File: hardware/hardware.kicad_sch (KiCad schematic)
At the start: 34 parts, among them J1 Conn_01x02, Q1 AON6500, Q2 AON6500, Q3 AON6500, Q4 AON6500, Q5 AON6500, Q6 AON6500, U1 CH32M007G8R6

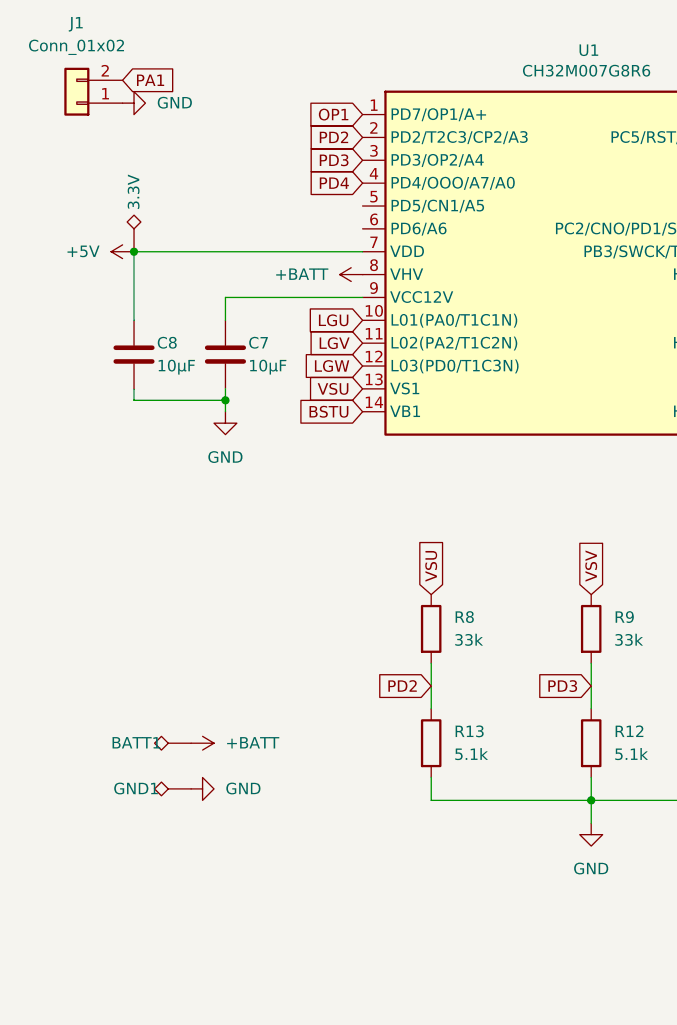
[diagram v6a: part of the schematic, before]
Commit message: add battery capacitor
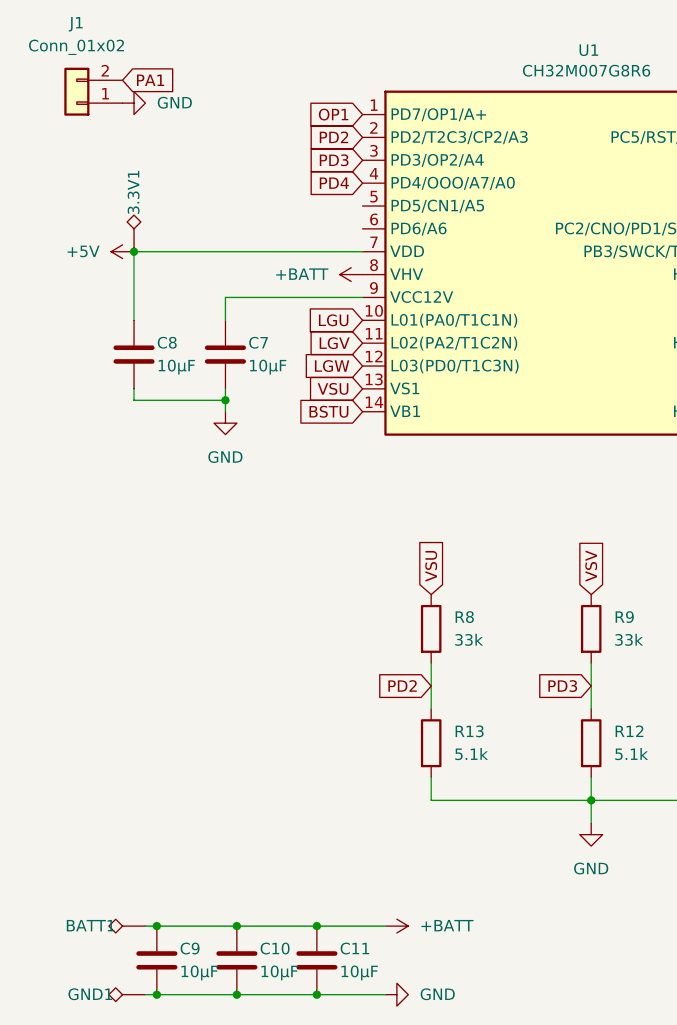
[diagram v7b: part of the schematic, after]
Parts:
- added C10, C11, C9: 10µF, Capacitor_SMD:C_1206_3216Metric, symbol Device:C
- renumbered 3.3V to 3.3V1
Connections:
- net +BATT: now also C10.2, C11.2, C9.2
- net GND: now also C10.1, C11.1, C9.1
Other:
- moved on the sheet: BATT1, GND1

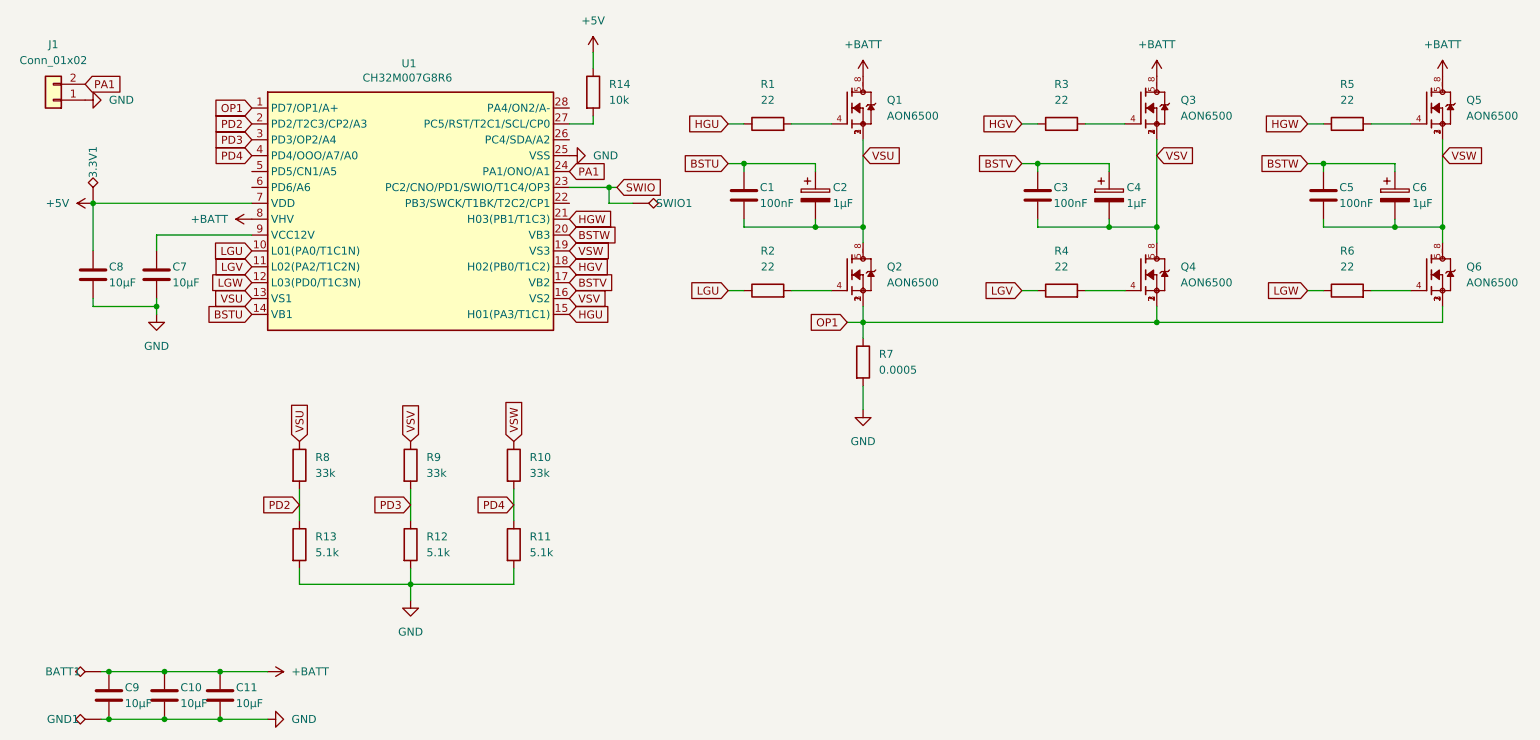
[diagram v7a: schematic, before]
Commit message: update capacitor
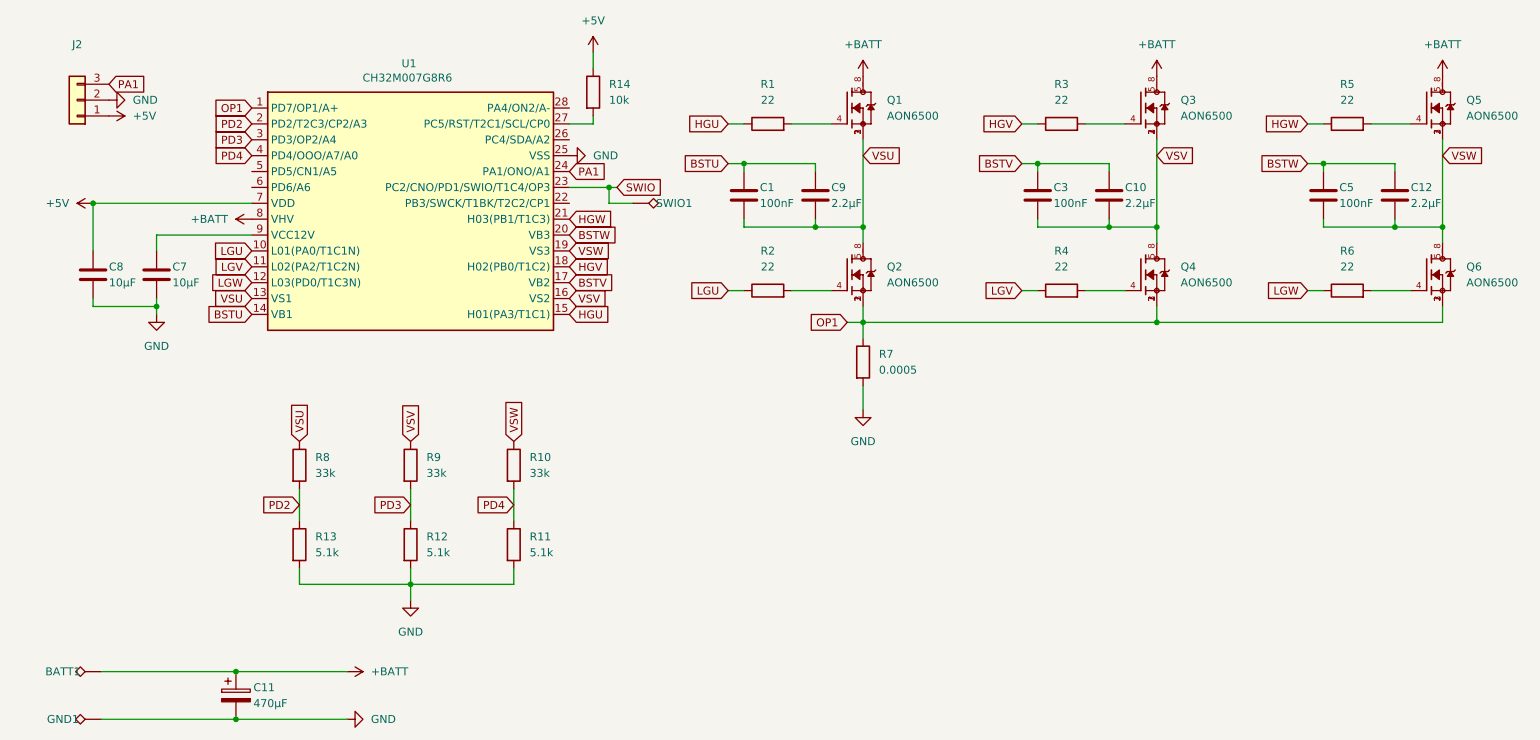
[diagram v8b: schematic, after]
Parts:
- removed 3.3V1: TestPoint_Alt, TestPoint:TestPoint_Pad_1.5x1.5mm, symbol Connector:TestPoint_Alt
- removed C11: 10µF, Capacitor_SMD:C_1206_3216Metric, symbol Device:C
- removed C2, C4, C6: 1µF, Capacitor_SMD:CP_Elec_4x4.5, symbol Device:C_Polarized
- removed J1: Conn_01x02, Connector_PinHeader_2.54mm:PinHeader_1x02_P2.54mm_Vertical, symbol Connector_Generic:Conn_01x02
- added C11: 470µF, Capacitor_THT:CP_Radial_D10.0mm_P5.00mm, symbol Device:C_Polarized
- added C12: 2.2µF, Capacitor_SMD:C_1206_3216Metric, symbol Device:C
- added J2: Conn_01x03, Connector_PinHeader_2.54mm:PinHeader_1x03_P2.54mm_Vertical, symbol Connector_Generic:Conn_01x03
- C10, C9: value 10µF -> 2.2µF
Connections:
- net +5V: now also J2.1 (Pin_1)
- net +BATT: now also C11.1; no longer C10.2, C9.2
- net BSTU: now also C9.2
- net BSTV: now also C10.2
- net BSTW: now also C12.2
- net GND: now also C11.2, J2.2 (Pin_2); no longer C10.1, C9.1
- net PA1: now also J2.3 (Pin_3)
- net VSU: now also C9.1
- net VSV: now also C10.1
- net VSW: now also C12.1
